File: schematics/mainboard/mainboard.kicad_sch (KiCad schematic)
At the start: 94 parts, among them J1 SD_Card_Receptacle, J2 LCD_CONN, J3 USB_C_Receptacle_USB2.0_16P, J4 BATTERY_CONN, J6 HID_CONN, J7 SPEAKER, J8 TRACKBALL_CONN, J9 AudioJack3, P1 1-1473005-4, SW1 SW_SPST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

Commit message: Added "button board". Also placed LCD on main board at correct location.
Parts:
- added R20: 10k, Resistor_SMD:R_0805_2012Metric_Pad1.20x1.40mm_HandSolder, symbol Device:R
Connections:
- net 3V3: now also R20.2
- net HIO_BTN_RESET: now reaches J6.11 (Pin_11)
- net HIO_BTN_RESET: now also P1.78, R20.1
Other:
- moved on the sheet: J6
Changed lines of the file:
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@@
 	)
 	(junction
+		(at 80.01 513.08)
+		(diameter 0)
+		(color 0 0 0 0)
+	)
+	(junction
+		(at 82.55 557.53)
+		(diameter 0)
+		(color 0 0 0 0)
+	)
+	(junction
 		(at 603.25 69.85)
 		(diameter 0)
@@
 	(wire
 		(pts
-			(xy 85.09 524.51) (xy 85.09 532.13)
+			(xy 91.44 524.51) (xy 91.44 532.13)
 		)
 		(stroke
@@
 	(wire
 		(pts
-			(xy 87.63 544.83) (xy 69.85 544.83)
+			(xy 95.25 544.83) (xy 69.85 544.83)
 		)
 		(stroke
@@
 	(wire
 		(pts
-			(xy 87.63 537.21) (xy 62.23 537.21)
+			(xy 95.25 537.21) (xy 62.23 537.21)
 		)
 		(stroke
@@
 	(wire
 		(pts
+			(xy 55.88 557.53) (xy 82.55 557.53)
+		)
+		(stroke
+			(width 0)
+			(type default)
+		)
+	)
+	(wire
+		(pts
 			(xy 208.28 82.55) (xy 208.28 83.82)
 		)
@@
 	(wire
 		(pts
-			(xy 87.63 547.37) (xy 72.39 547.37)
+			(xy 95.25 547.37) (xy 72.39 547.37)
 		)
 		(stroke
@@
 	(wire
 		(pts
-			(xy 87.63 549.91) (xy 74.93 549.91)
+			(xy 95.25 549.91) (xy 74.93 549.91)
 		)
 		(stroke
@@
 	(wire
 		(pts
-			(xy 87.63 534.67) (xy 59.69 534.67)
+			(xy 95.25 534.67) (xy 59.69 534.67)
 		)
 		(stroke
@@
 	(wire
 		(pts
-			(xy 87.63 552.45) (xy 77.47 552.45)
+			(xy 95.25 552.45) (xy 77.47 552.45)
 		)
 		(stroke
@@
 	(wire
 		(pts
+			(xy 82.55 557.53) (xy 95.25 557.53)
+		)
+		(stroke
+			(width 0)
+			(type default)
+		)
+	)
+	(wire
+		(pts
 			(xy 318.77 337.82) (xy 321.31 337.82)
 		)
@@
 	(wire
 		(pts
-			(xy 87.63 539.75) (xy 64.77 539.75)
+			(xy 95.25 539.75) (xy 64.77 539.75)
 		)
 		(stroke
@@
 	(wire
 		(pts
-			(xy 87.63 542.29) (xy 67.31 542.29)
+			(xy 95.25 542.29) (xy 67.31 542.29)
 		)
 		(stroke
@@
 	(wire
 		(pts
+			(xy 82.55 513.08) (xy 80.01 513.08)
+		)
+		(stroke
+			(width 0)
+			(type default)
+		)
+	)
+	(wire
+		(pts
 			(xy 102.87 184.15) (xy 105.41 184.15)
 		)
@@
 	(wire
 		(pts
-			(xy 87.63 554.99) (xy 80.01 554.99)
+			(xy 95.25 554.99) (xy 80.01 554.99)
 		)
 		(stroke
@@
 	(wire
 		(pts
+			(xy 351.79 365.76) (xy 355.6 365.76)
+		)
+		(stroke
+			(width 0)
+			(type default)
+		)
+	)
+	(wire
+		(pts
 			(xy 753.11 114.3) (xy 753.11 116.84)
 		)
@@
 	(wire
 		(pts
-			(xy 85.09 532.13) (xy 87.63 532.13)
+			(xy 91.44 532.13) (xy 95.25 532.13)
 		)
 		(stroke
@@
 	(wire
 		(pts
+			(xy 82.55 516.89) (xy 82.55 513.08)
+		)
+		(stroke
+			(width 0)
+			(type default)
+		)
+	)
+	(wire
+		(pts
 			(xy 648.97 168.91) (xy 648.97 175.26)
 		)
@@
 	(wire
 		(pts
+			(xy 82.55 524.51) (xy 82.55 557.53)
+		)
+		(stroke
+			(width 0)
+			(type default)
+		)
+	)
+	(wire
+		(pts
 			(xy 58.42 74.93) (xy 62.23 74.93)
 		)
@@
 		)
 	)
+	(global_label "HIO_BTN_RESET"
+		(shape output)
+		(at 55.88 557.53 180)
+		(fields_autoplaced yes)
+		(effects
+			(font
+				(size 1.27 1.27)
+			)
+			(justify right)
+		)
+		(property "Intersheetrefs" "${INTERSHEET_REFS}"
+			(at 38.3806 557.53 0)
+			(effects
+				(font
+					(size 1.27 1.27)
+				)
+				(justify right)
+				(hide yes)
+			)
+		)
+	)
 	(global_label "I2C_INTERRUPT"
 		(shape input)
@@
 		)
 	)
+	(global_label "HIO_BTN_RESET"
+		(shape output)
+		(at 355.6 365.76 0)
+		(fields_autoplaced yes)
+		(effects
+			(font
+				(size 1.27 1.27)
+			)
+			(justify left)
+		)
+		(property "Intersheetrefs" "${INTERSHEET_REFS}"
+			(at 373.0994 365.76 0)
+			(effects
+				(font
+					(size 1.27 1.27)
+				)
+				(justify left)
+				(hide yes)
+			)
+		)
+	)
 	(global_label "SRAM_D4"
 		(shape bidirectional)
@@
 	(symbol
 		(lib_id "Connector_Generic:Conn_01x12")
-		(at 92.71 544.83 0)
+		(at 100.33 544.83 0)
 		(unit 1)
 		(exclude_from_sim no)
@@
 		(fields_autoplaced yes)
 		(property "Reference" "J6"
-			(at 95.25 544.8299 0)
+			(at 102.87 544.8299 0)
 			(effects
 				(font
@@
 		)
 		(property "Value" "HID_CONN"
-			(at 95.25 547.3699 0)
+			(at 102.87 547.3699 0)
 			(effects
 				(font
@@
 		)
 		(property "Footprint" "Connector_PinHeader_2.54mm:PinHeader_1x12_P2.54mm_Vertical"
-			(at 92.71 544.83 0)
+			(at 100.33 544.83 0)
 			(effects
 				(font
@@
 		)
 		(property "Datasheet" "~"
-			(at 92.71 544.83 0)
+			(at 100.33 544.83 0)
 			(effects
 				(font
@@
 		)
 		(property "Description" "Generic connector, single row, 01x12, script generated (kicad-library-utils/schlib/autogen/connector/)"
-			(at 92.71 544.83 0)
+			(at 100.33 544.83 0)
 			(effects
 				(font
@@
 	)
 	(symbol
+		(lib_id "Device:R")
+		(at 82.55 520.7 180)
+		(unit 1)
+		(exclude_from_sim no)
+		(in_bom yes)
+		(on_board yes)
+		(dnp no)
+		(property "Reference" "R20"
+			(at 80.01 522.224 90)
+			(effects
+				(font
+					(size 1.27 1.27)
+				)
+			)
+		)
+		(property "Value" "10k"
+			(at 80.01 518.668 90)
+			(effects
+				(font
+					(size 1.27 1.27)
+				)
+			)
+		)
+		(property "Footprint" "Resistor_SMD:R_0805_2012Metric_Pad1.20x1.40mm_HandSolder"
+			(at 84.328 520.7 90)
+			(effects
+				(font
+					(size 1.27 1.27)
+				)
+				(hide yes)
+			)
+		)
+		(property "Datasheet" "~"
+			(at 82.55 520.7 0)
+			(effects
+				(font
+					(size 1.27 1.27)
+				)
+				(hide yes)
+			)
+		)
+		(property "Description" "Resistor"
+			(at 82.55 520.7 0)
+			(effects
+				(font
+					(size 1.27 1.27)
+				)
+				(hide yes)
+			)
+		)
+		(pin "1"
+		)
+		(pin "2"
+		)
+		(instances
+			(project "mainboard"
+				(path "/cefc859f-34fb-418b-9c7c-f7e62c11b64f"
+					(reference "R20")
+					(unit 1)
+				)
+			)
+		)
+	)
+	(symbol
 		(lib_id "power:GND")
 		(at 66.04 441.96 270)
@@
 	(symbol
 		(lib_id "power:GND")
-		(at 85.09 524.51 180)
+		(at 91.44 524.51 180)
 		(unit 1)
 		(exclude_from_sim no)
@@
 		(dnp no)
 		(property "Reference" "#PWR056"
-			(at 85.09 518.16 0)
+			(at 91.44 518.16 0)
 			(effects
 				(font
@@
 		)
 		(property "Value" "GND"
-			(at 85.0899 520.7 90)
+			(at 91.4399 520.7 90)
 			(effects
 				(font
@@
 		)
 		(property "Footprint" ""
-			(at 85.09 524.51 0)
+			(at 91.44 524.51 0)
 			(effects
 				(font
@@
 		)
 		(property "Datasheet" ""
-			(at 85.09 524.51 0)
+			(at 91.44 524.51 0)
 			(effects
 				(font
@@
 		)
 		(property "Description" "Power symbol creates a global label with name \"GND\" , ground"
-			(at 85.09 524.51 0)
+			(at 91.44 524.51 0)
 			(effects
 				(font

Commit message: Flat flex connector for interconnect.
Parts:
- removed J6: HID_CONN, Connector_PinHeader_2.54mm:PinHeader_1x12_P2.54mm_Vertical, symbol Connector_Generic:Conn_01x12
- removed J8: TRACKBALL_CONN, Connector_PinHeader_2.54mm:PinHeader_1x05_P2.54mm_Vertical, symbol Connector_Generic:Conn_01x05
- added J5: 527461671, CON_527461671_MOL, symbol CON_527461671_MOL:527461671
- R10, R11, R12, R13, R14, R15, R16, R20, R30, R31, R8, R9: footprint Resistor_SMD:R_0805_2012Metric_Pad1.20x1.40mm_HandSolder -> Resistor_SMD:R_0603_1608Metric_Pad0.98x0.95mm_HandSolder
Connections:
- net 3V3: now also J5.P2
- net GND: now also J5.1
- net HIO_BTN_A: now also P1.86, J5.6; no longer P1.88
- net HIO_BTN_B: now also P1.88, J5.7; no longer P1.86
- net HIO_BTN_C: now also P1.90, J5.8; no longer P1.84
- net HIO_BTN_D: now also P1.92, J5.9; no longer P1.82
- net HIO_BTN_RESET: now also P1.96, J5.11; no longer P1.78
- net HIO_BTN_X: now also P1.94, J5.10; no longer P1.80
- net HIO_DPAD_E: now also P1.84, J5.5; no longer P1.90
- net HIO_DPAD_N: now also P1.78, J5.2; no longer P1.96
- net HIO_DPAD_S: now also P1.80, J5.3; no longer P1.94
- net HIO_DPAD_W: now also P1.82, J5.4; no longer P1.92
- net I2C_INTERRUPT: now also J5.14
- net I2C_SCL: now also J5.13
- net I2C_SDA: now also J5.12
- no-connect marks 74 -> 77
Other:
- moved on the sheet: C8, R10, R11, R12, R13, R14, R15, R16, R20, R30, R31, R8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

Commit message: Some cleanup in mainboard.
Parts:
- R1, R17, R18, R19, R2, R21, R22, R23, R24, R25, R26, R27, R28, R29, R3, R4, R6, R7: footprint Resistor_SMD:R_0805_2012Metric_Pad1.20x1.40mm_HandSolder -> Resistor_SMD:R_0603_1608Metric_Pad0.98x0.95mm_HandSolder
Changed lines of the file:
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@@
 			)
 		)
-		(property "Footprint" "Resistor_SMD:R_0805_2012Metric_Pad1.20x1.40mm_HandSolder"
+		(property "Footprint" "Resistor_SMD:R_0603_1608Metric_Pad0.98x0.95mm_HandSolder"
 			(at 132.08 404.622 90)
 			(effects
@@
 			)
 		)
-		(property "Footprint" "Resistor_SMD:R_0805_2012Metric_Pad1.20x1.40mm_HandSolder"
+		(property "Footprint" "Resistor_SMD:R_0603_1608Metric_Pad0.98x0.95mm_HandSolder"
 			(at 210.058 78.74 90)
 			(effects
@@
 			)
 		)
-		(property "Footprint" "Resistor_SMD:R_0805_2012Metric_Pad1.20x1.40mm_HandSolder"
+		(property "Footprint" "Resistor_SMD:R_0603_1608Metric_Pad0.98x0.95mm_HandSolder"
 			(at 311.658 46.99 90)
 			(effects
@@
 			)
 		)
-		(property "Footprint" "Resistor_SMD:R_0805_2012Metric_Pad1.20x1.40mm_HandSolder"
+		(property "Footprint" "Resistor_SMD:R_0603_1608Metric_Pad0.98x0.95mm_HandSolder"
 			(at 591.312 166.37 90)
 			(effects
@@
 			)
 		)
-		(property "Footprint" "Resistor_SMD:R_0805_2012Metric_Pad1.20x1.40mm_HandSolder"
+		(property "Footprint" "Resistor_SMD:R_0603_1608Metric_Pad0.98x0.95mm_HandSolder"
 			(at 112.522 457.2 90)
 			(effects
@@
 			)
 		)
-		(property "Footprint" "Resistor_SMD:R_0805_2012Metric_Pad1.20x1.40mm_HandSolder"
+		(property "Footprint" "Resistor_SMD:R_0603_1608Metric_Pad0.98x0.95mm_HandSolder"
 			(at 71.882 463.55 90)
 			(effects
@@
 			)
 		)
-		(property "Footprint" "Resistor_SMD:R_0805_2012Metric_Pad1.20x1.40mm_HandSolder"
+		(property "Footprint" "Resistor_SMD:R_0603_1608Metric_Pad0.98x0.95mm_HandSolder"
 			(at 647.192 165.1 90)
 			(effects
@@
 			)
 		)
-		(property "Footprint" "Resistor_SMD:R_0805_2012Metric_Pad1.20x1.40mm_HandSolder"
+		(property "Footprint" "Resistor_SMD:R_0603_1608Metric_Pad0.98x0.95mm_HandSolder"
 			(at 53.34 122.428 90)
 			(effects
@@
 			)
 		)
-		(property "Footprint" "Resistor_SMD:R_0805_2012Metric_Pad1.20x1.40mm_HandSolder"
+		(property "Footprint" "Resistor_SMD:R_0603_1608Metric_Pad0.98x0.95mm_HandSolder"
 			(at 202.438 78.74 90)
 			(effects
@@
 			)
 		)
-		(property "Footprint" "Resistor_SMD:R_0805_2012Metric_Pad1.20x1.40mm_HandSolder"
+		(property "Footprint" "Resistor_SMD:R_0603_1608Metric_Pad0.98x0.95mm_HandSolder"
 			(at 269.748 46.99 90)
 			(effects
@@
 			)
 		)
-		(property "Footprint" "Resistor_SMD:R_0805_2012Metric_Pad1.20x1.40mm_HandSolder"
+		(property "Footprint" "Resistor_SMD:R_0603_1608Metric_Pad0.98x0.95mm_HandSolder"
 			(at 132.08 417.322 90)
 			(effects
@@
 			)
 		)
-		(property "Footprint" "Resistor_SMD:R_0805_2012Metric_Pad1.20x1.40mm_HandSolder"
+		(property "Footprint" "Resistor_SMD:R_0603_1608Metric_Pad0.98x0.95mm_HandSolder"
 			(at 264.668 46.99 90)
 			(effects
@@
 			)
 		)
-		(property "Footprint" "Resistor_SMD:R_0805_2012Metric_Pad1.20x1.40mm_HandSolder"
+		(property "Footprint" "Resistor_SMD:R_0603_1608Metric_Pad0.98x0.95mm_HandSolder"
 			(at 249.428 46.99 90)
 			(effects
@@
 			)
 		)
-		(property "Footprint" "Resistor_SMD:R_0805_2012Metric_Pad1.20x1.40mm_HandSolder"
+		(property "Footprint" "Resistor_SMD:R_0603_1608Metric_Pad0.98x0.95mm_HandSolder"
 			(at 259.588 46.99 90)
 			(effects
@@
 			)
 		)
-		(property "Footprint" "Resistor_SMD:R_0805_2012Metric_Pad1.20x1.40mm_HandSolder"
+		(property "Footprint" "Resistor_SMD:R_0603_1608Metric_Pad0.98x0.95mm_HandSolder"
 			(at 64.262 463.55 90)
 			(effects
@@
 			)
 		)
-		(property "Footprint" "Resistor_SMD:R_0805_2012Metric_Pad1.20x1.40mm_HandSolder"
+		(property "Footprint" "Resistor_SMD:R_0603_1608Metric_Pad0.98x0.95mm_HandSolder"
 			(at 53.34 119.888 90)
 			(effects
@@
 			)
 		)
-		(property "Footprint" "Resistor_SMD:R_0805_2012Metric_Pad1.20x1.40mm_HandSolder"
+		(property "Footprint" "Resistor_SMD:R_0603_1608Metric_Pad0.98x0.95mm_HandSolder"
 			(at 640.842 165.1 90)
 			(effects
@@
 			)
 		)
-		(property "Footprint" "Resistor_SMD:R_0805_2012Metric_Pad1.20x1.40mm_HandSolder"
+		(property "Footprint" "Resistor_SMD:R_0603_1608Metric_Pad0.98x0.95mm_HandSolder"
 			(at 254.508 46.99 90)
 			(effects

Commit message: Added load switch to mainboard to control startup.
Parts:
- added C39: 47uF, Capacitor_SMD:CP_Elec_5x5.3, symbol Device:C_Polarized
- added C41: 200pF, Capacitor_SMD:C_0805_2012Metric, symbol Device:C
- added R32: ~, Resistor_SMD:R_0603_1608Metric_Pad0.98x0.95mm_HandSolder, symbol Device:R
- added U9: TPS22917DBV, Package_TO_SOT_SMD:SOT-23-6, symbol Power_Management:TPS22917DBV
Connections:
- net 3V3_AUDIO: now also C39.1
- net GND: now also C39.2, C41.1, U9.2 (GND)
- net SYS_LOAD: now also R32.1, U9.6 (VOUT); no longer SW1.2 (B)
- net at C28.2, R26.1, R27.1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: now also U9.1 (VIN)
- new net: SW1.2 (B), U9.3 (ON)
- new net: C41.2, U9.4 (CT)
- new net: R32.2, U9.5 (QOD)
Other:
- moved on the sheet: C3, J1, R21, R22, R23, R24, R25, R29, SW1

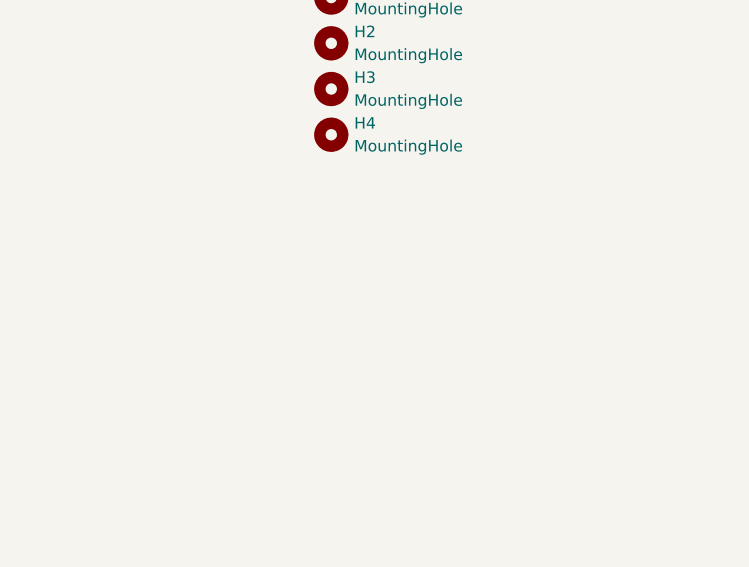
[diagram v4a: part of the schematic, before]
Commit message: Mounting points for mainboard added. Adjusted position of track ball on buttboard.
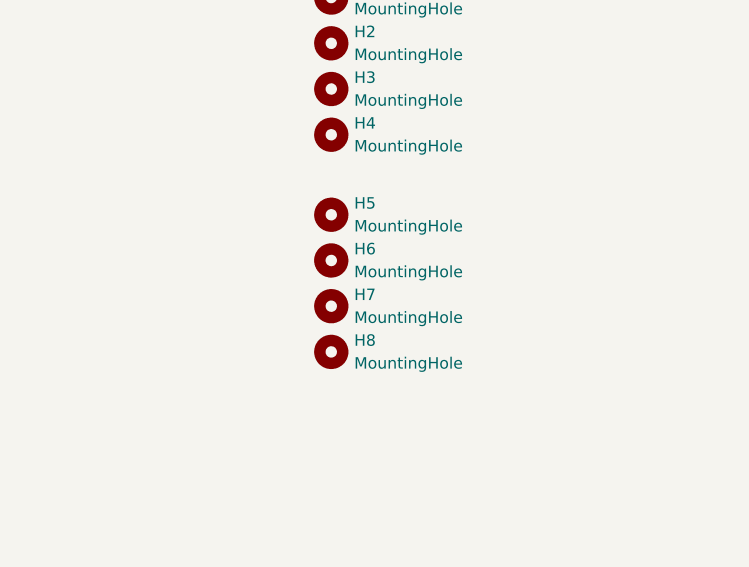
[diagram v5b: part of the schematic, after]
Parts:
- added H5, H6, H7, H8: MountingHole, MountingHole:MountingHole_2.5mm, symbol Mechanical:MountingHole

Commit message: Schematic work; I2C shared with trackball and audio chip.
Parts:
- removed R18, R19: 4k7, Resistor_SMD:R_0603_1608Metric_Pad0.98x0.95mm_HandSolder, symbol Device:R
- removed R30, R31: 1k2, Resistor_SMD:R_0603_1608Metric_Pad0.98x0.95mm_HandSolder, symbol Device:R
- added R33, R34: 4k7, Resistor_SMD:R_0603_1608Metric_Pad0.98x0.95mm_HandSolder, symbol Device:R
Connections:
- net AUDIO_SCL is gone; now on net I2C_SCL: U8.10 (SCL)
- net AUDIO_SDA is gone; now on net I2C_SDA: U8.9 (SDA)
- net 3V3: now also R33.1, R34.1
- net AUDIO_BCLK: now also P1.68
- net AUDIO_DIN: now also P1.64
- net AUDIO_MCLK: now also P1.70
- net AUDIO_WCLK: now also P1.66
- net I2C_SCL: now also R33.2
- net I2C_SDA: now also R34.2
- net SD_CARD: now also P1.54
- net I2C_INTERRUPT renamed TRACKBALL_INTERRUPT

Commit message: Audio interrupt connected to SODIMM connector.
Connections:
- net GPIO1 is gone; now on net AUDIO_INTERRUPT: U8.32 (GPIO1)
- net AUDIO_INTERRUPT: now reaches P1.72
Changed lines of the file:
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@@
 	(wire
 		(pts
+			(xy 351.79 358.14) (xy 355.6 358.14)
+		)
+		(stroke
+			(width 0)
+			(type default)
+		)
+	)
+	(wire
+		(pts
 			(xy 190.5 449.58) (xy 209.55 449.58)
 		)
@@
 		)
 	)
-	(global_label "GPIO1"
-		(shape bidirectional)
-		(at 717.55 190.5 0)
-		(fields_autoplaced yes)
-		(effects
-			(font
-				(size 1.27 1.27)
-			)
-			(justify left)
-		)
-		(property "Intersheetrefs" "${INTERSHEET_REFS}"
-			(at 725.5547 190.5 0)
-			(effects
-				(font
-					(size 1.27 1.27)
-				)
-				(justify left)
-				(hide yes)
-			)
-		)
-	)
 	(global_label "SVDD1"
 		(shape output)
@@
 		)
 	)
+	(global_label "AUDIO_INTERRUPT"
+		(shape input)
+		(at 355.6 358.14 0)
+		(fields_autoplaced yes)
+		(effects
+			(font
+				(size 1.27 1.27)
+			)
+			(justify left)
+		)
+		(property "Intersheetrefs" "${INTERSHEET_REFS}"
+			(at 375.3372 358.14 0)
+			(effects
+				(font
+					(size 1.27 1.27)
+				)
+				(justify left)
+				(hide yes)
+			)
+		)
+	)
 	(global_label "SRAM_D1"
 		(shape bidirectional)
@@
 			(effects
 				(font
+					(size 1.27 1.27)
+				)
+				(justify left)
+				(hide yes)
+			)
+		)
+	)
+	(global_label "AUDIO_INTERRUPT"
+		(shape output)
+		(at 717.55 190.5 0)
+		(fields_autoplaced yes)
+		(effects
+			(font
+				(size 1.27 1.27)
+			)
+			(justify left)
+		)
+		(property "Intersheetrefs" "${INTERSHEET_REFS}"
+			(at 737.2872 190.5 0)
+			(effects
+				(font

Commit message: Some work on the mainboard.
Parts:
- removed J7: SPEAKER, Connector_PinHeader_2.54mm:PinHeader_1x02_P2.54mm_Vertical, symbol Connector:Conn_01x02_Pin
- added C40: 47uF, Capacitor_SMD:CP_Elec_5x5.3, symbol Device:C_Polarized
- added J6: SPEAKER_CONN, Connector_JST:JST_PH_S2B-PH-K_1x02_P2.00mm_Horizontal, symbol Connector_Generic:Conn_01x02
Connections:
- net 3V3_AUDIO: now also C40.1
- net GND: now also C40.2
- net at U8.19 (SPKM), U8.23 (SPKM): now also J6.2 (Pin_2)
- net at U8.22 (SPKP), U8.26 (SPKP): now also J6.1 (Pin_1)
